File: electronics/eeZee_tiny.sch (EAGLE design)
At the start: 8 parts, among them IC1 ATtiny, J2 avrisp

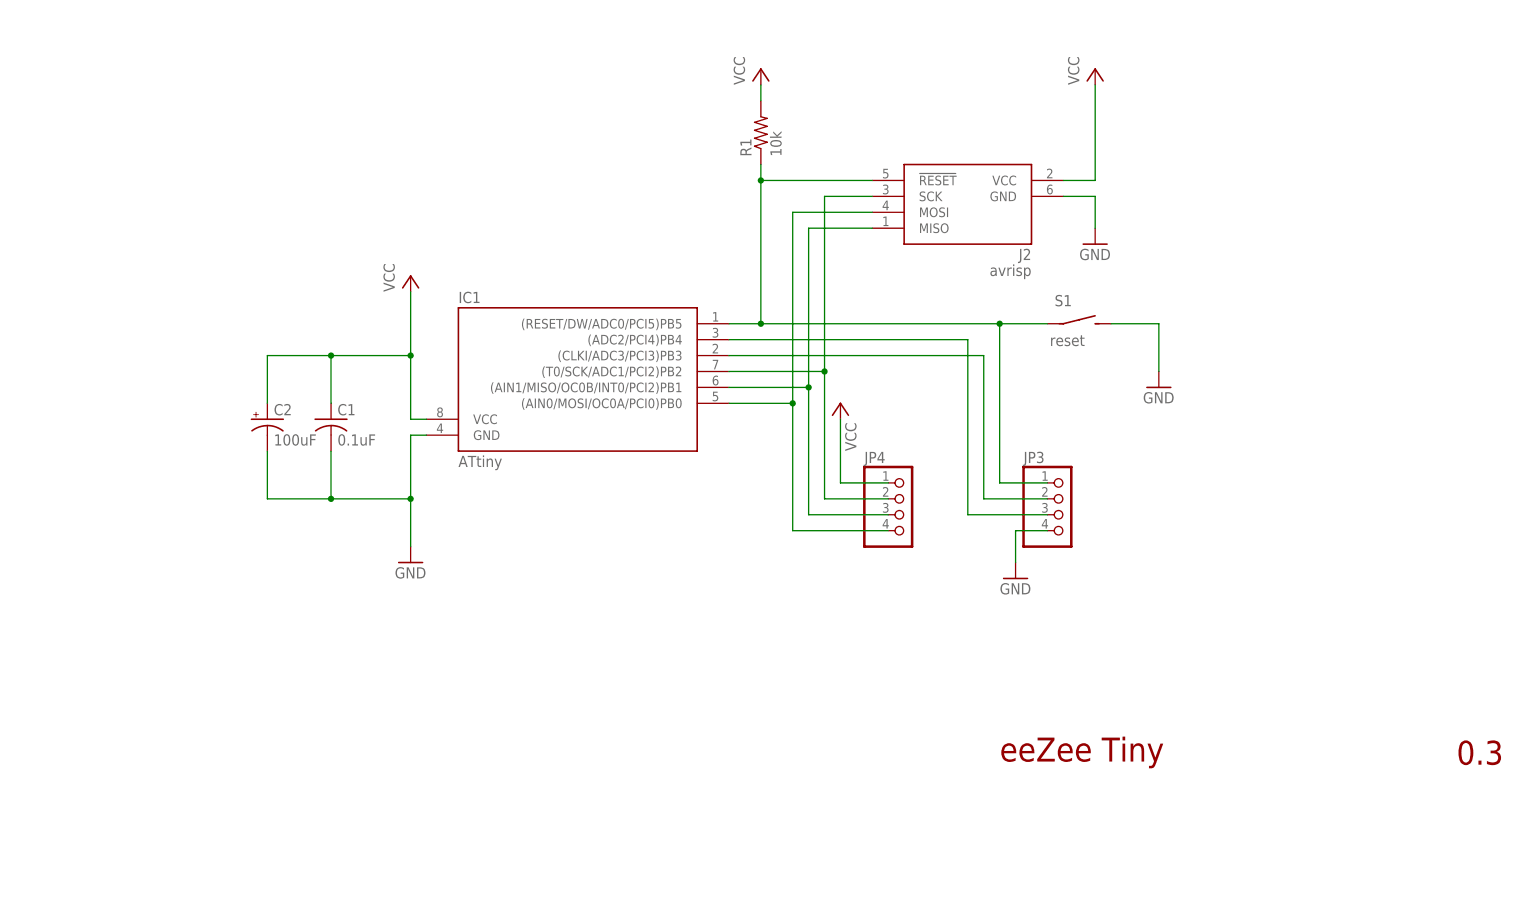
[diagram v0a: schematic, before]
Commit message: revised 8pdip pads, rerouted avrisp traces, changed passives layout, changed main cap from 100u to 10u and changed to 1206 pkg, replaced attiny13 with attiny25 from bt library, changed avrisp to version from bt library, changed logo, added cc-by-sa, added documentation url
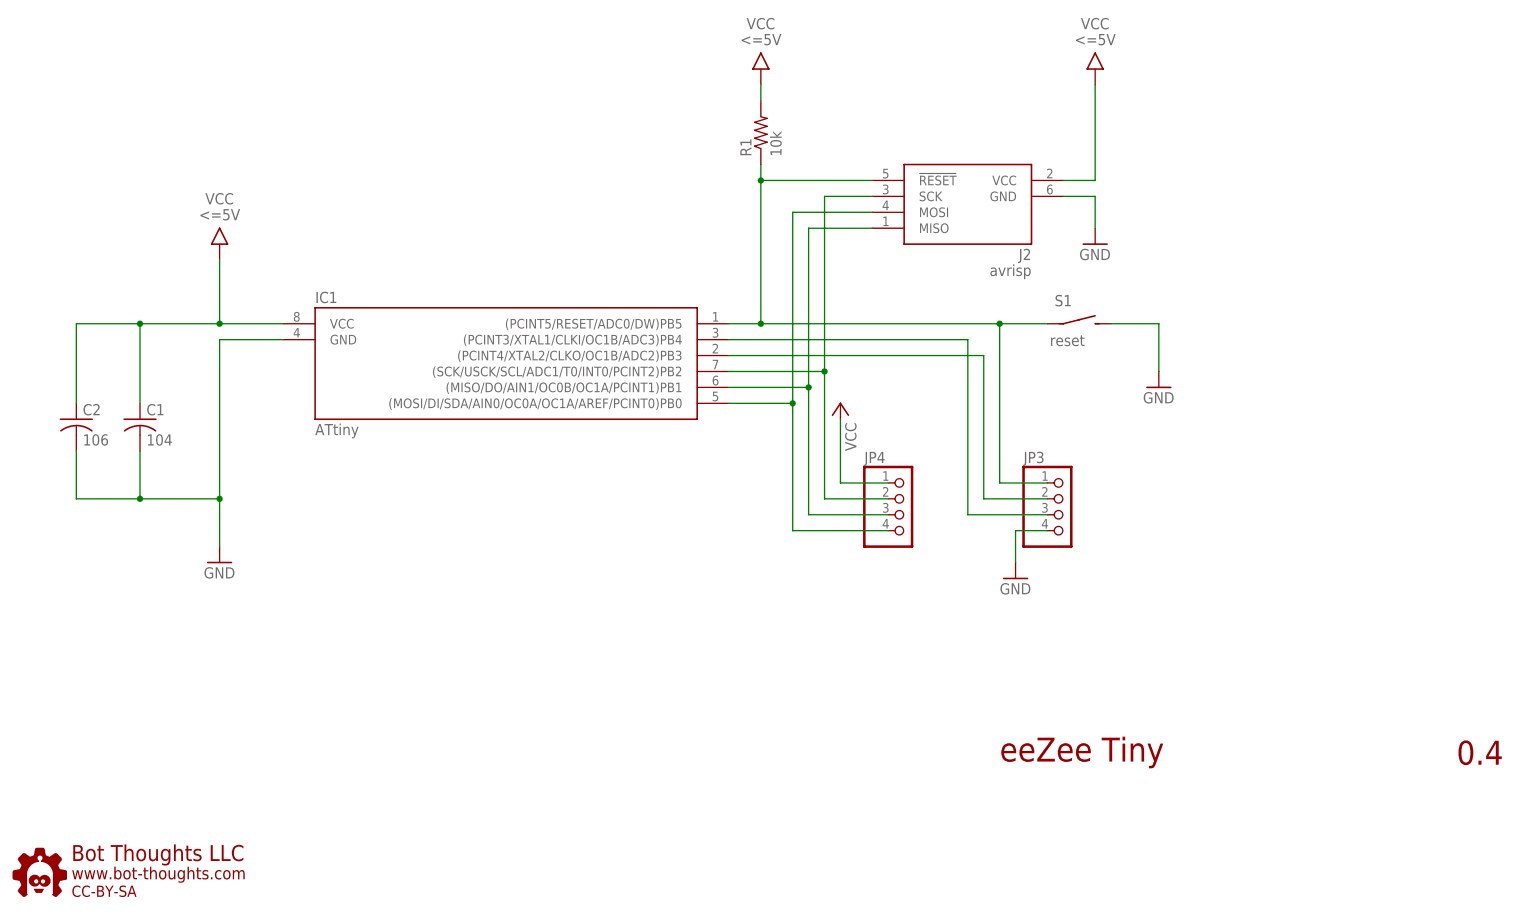
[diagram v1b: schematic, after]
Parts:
- added U$1: BTLOGO-LOGO-MD, bt:BTLOGO-LOGO-MD
- C1: value 0.1uF -> 104
- C2: value 100uF -> 106; device mes_rcl:CAP_POL_SMC_B -> rcl:C-USC1206
- IC1: device avr:ATTINY13-20P -> bt_avr:TINY25-20PU; PARTNO A08-LC-TT-R -> (none)
- J2: device ads4:AVRISP6 -> bt_avr:AVRISP6_COMPACT
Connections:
- removed net N$2: IC1.(CLKI/ADC3/PCI3)PB3, JP3.2
- removed net N$8: IC1.(ADC2/PCI4)PB4, JP3.3
- new net PB3: IC1.(PCINT4/XTAL2/CLKO/OC1B/ADC2)PB3, JP3.2
- new net PB4: IC1.(PCINT3/XTAL1/CLKI/OC1B/ADC3)PB4, JP3.3
- net !RESET: now also IC1.(PCINT5/RESET/ADC0/DW)PB5; no longer IC1.(RESET/DW/ADC0/PCI5)PB5
- net GND: now also C2.2; no longer C2.-
- net MISO: now also IC1.(MISO/DO/AIN1/OC0B/OC1A/PCINT1)PB1; no longer IC1.(AIN1/MISO/OC0B/INT0/PCI2)PB1
- net MOSI: now also IC1.(MOSI/DI/SDA/AIN0/OC0A/OC1A/AREF/PCINT0)PB0; no longer IC1.(AIN0/MOSI/OC0A/PCI0)PB0
- net SCK: now also IC1.(SCK/USCK/SCL/ADC1/T0/INT0/PCINT2)PB2; no longer IC1.(T0/SCK/ADC1/PCI2)PB2
- net VCC: now also C2.1; no longer C2.+
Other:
- note added: "0.4"
- note removed: "0.3"
- moved on the sheet: C1
